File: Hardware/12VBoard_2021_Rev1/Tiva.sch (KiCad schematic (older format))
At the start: 2 parts

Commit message: Added Component Values.
Added values to high side buck and
 footprints to components.
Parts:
- renumbered Conn2 to Conn1, Conn3 to Conn2
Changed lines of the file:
@@
 	6150 2250 5800 2250
 $Comp
-L MRDT_Connectors:Molex_SL_05 Conn2
+L MRDT_Connectors:Molex_SL_05 Conn1
 U 1 1 5F976F73
 P 6350 1900
-F 0 "Conn2" H 6300 1850 60  0000 L CNN
+F 0 "Conn1" H 6300 1850 60  0000 L CNN
 F 1 "Molex_SL_05" H 6200 1750 60  0000 L CNN
 F 2 "MRDT_Connectors:MOLEX_SL_05_Horizontal" H 6350 1900 60  0001 C CNN
@@
 $EndComp
 $Comp
-L MRDT_Connectors:Molex_SL_07 Conn3
+L MRDT_Connectors:Molex_SL_07 Conn2
 U 1 1 5F97771C
 P 6350 2900
-F 0 "Conn3" H 6350 2850 60  0000 L CNN
+F 0 "Conn2" H 6350 2850 60  0000 L CNN
 F 1 "Molex_SL_07" H 6200 2750 60  0000 L CNN
 F 2 "MRDT_Connectors:MOLEX_SL_07_Horizontal" H 6350 3100 60  0001 C CNN

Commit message: Added Logic power circuits (High)
Added three smaller bucks for high current logic power and seprated acuation and logic pp
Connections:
- net DriveCTL: now reaches Conn2.7
- no-connect marks 1 -> 0
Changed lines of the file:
@@
 Text Notes 6450 1872 0    50   ~ 0
 Gimbal Sense (Analog Read)
-NoConn ~ 6150 2850
+Text HLabel 5800 2850 0    50   Output ~ 0
+DriveCTL
+Wire Wire Line
+	6150 2850 5800 2850
 $EndSCHEMATC

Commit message: Layout Started
Board dimensions
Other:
- note added: "Drive Board CTL (Digital Write)"
- note added: "Tiva 4 analog(current sense)/ \n7 toggles(digital write)"
- note removed: "Tiva 4 analog(current sense)/ \n5 toggles(digital write)"
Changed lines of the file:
@@
 $Descr A4 11693 8268
 encoding utf-8
-Sheet 2 8
+Sheet 8 8
 Title ""
 Date ""
@@
 $EndDescr
 Text Notes 5650 3450 0    79   ~ 0
-Tiva 4 analog(current sense)/ \n5 toggles(digital write)
+Tiva 4 analog(current sense)/ \n7 toggles(digital write)
 Text Notes 7480 1490 2    50   ~ 0
 Drive Sense (Analog Read)
@@
 Wire Wire Line
 	6150 2850 5800 2850
+Text Notes 7645 2880 2    50   ~ 0
+Drive Board CTL (Digital Write)
 $EndSCHEMATC

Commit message: Checked H pins
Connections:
- net DriveSense: no longer names the net of Conn1.1
- net MulitmediaSense renamed MultimediaSense
- no-connect marks 0 -> 1
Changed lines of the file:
@@
 EESchema Schematic File Version 4
-LIBS:12VBoard_2021_Rev1-cache
 EELAYER 30 0
 EELAYER END
@@
 Text Notes 6459 2385 0    49   ~ 0
 Gimbal CTL (Digital Write)
-Text HLabel 5800 1450 0    49   Input ~ 0
-DriveSense
-Wire Wire Line
-	6150 1450 5800 1450
 Text HLabel 5800 1550 0    49   Input ~ 0
 AuxMountSense
@@
 	6150 1550 5800 1550
 Text HLabel 5800 1650 0    49   Input ~ 0
-MulitmediaSense
+MultimediaSense
 Wire Wire Line
 	6150 1650 5800 1650
@@
 Text Notes 7645 2880 2    50   ~ 0
 Drive Board CTL (Digital Write)
+NoConn ~ 6150 1450
 $EndSCHEMATC

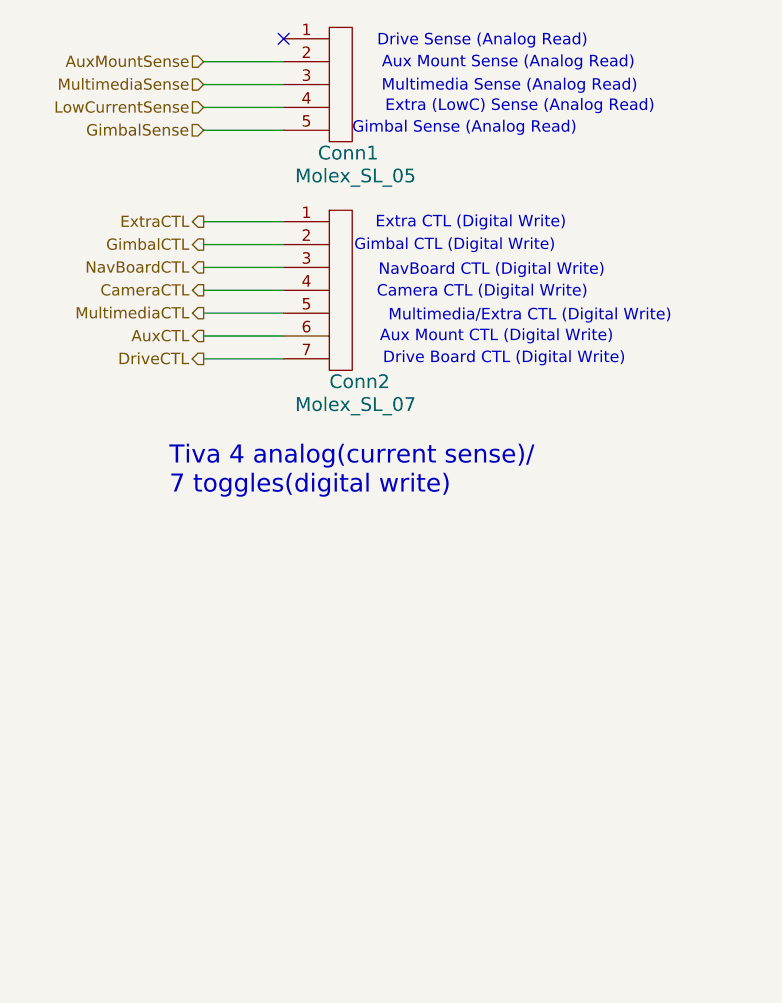
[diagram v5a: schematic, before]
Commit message: Changes!
Added the new correct connectors and redid all signal lines to the High Current side of the board. Also deleted all uncessacary components on the High current side that are no longer used.
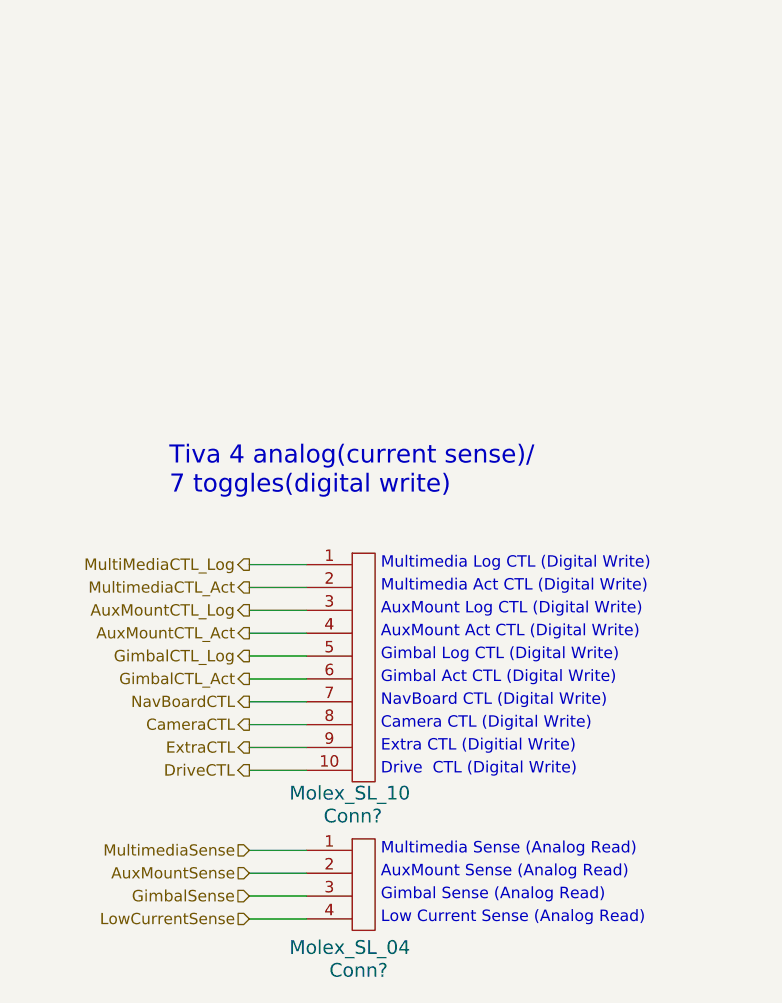
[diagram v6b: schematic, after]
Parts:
- removed Conn1: Molex_SL_05, MRDT_Connectors:MOLEX_SL_05_Horizontal, symbol MRDT_Connectors:Molex_SL_05
- removed Conn2: Molex_SL_07, MRDT_Connectors:MOLEX_SL_07_Horizontal, symbol MRDT_Connectors:Molex_SL_07
- added Conn?: Molex_SL_10, symbol MRDT_Connectors:Molex_SL_10
- added Conn?: Molex_SL_04, symbol MRDT_Connectors:Molex_SL_04
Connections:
- net AuxMountSense: now also Conn?.2
- net CameraCTL: now also Conn?.8
- net DriveCTL: now also Conn?.10
- net ExtraCTL: now also Conn?.9
- net GimbalSense: now also Conn?.3
- net LowCurrentSense: now also Conn?.4
- net MultimediaSense: now also Conn?.1
- net NavBoardCTL: now also Conn?.7
- new net AuxMountCTL_Act: Conn?.4
- new net AuxMountCTL_Log: Conn?.3
- new net GimbalCTL_Act: Conn?.6
- new net GimbalCTL_Log: Conn?.5
- new net MultiMediaCTL_Log: Conn?.1
- new net MultimediaCTL_Act: Conn?.2
- no-connect marks 1 -> 0
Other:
- note added: "AuxMount Act CTL (Digital Write)"
- note added: "AuxMount Log CTL (Digital Write)"
- note added: "AuxMount Sense (Analog Read)"
- note added: "Drive CTL (Digital Write)\n"
- note added: "Extra CTL (Digitial Write)"
- note added: "Gimbal Act CTL (Digital Write)"
- note added: "Gimbal Log CTL (Digital Write)"
- note added: "Low Current Sense (Analog Read)"
- note added: "Multimedia Act CTL (Digital Write)"
- note added: "Multimedia Log CTL (Digital Write)"
- note added: "Multimedia Sense (Analog Read)\n"
- note removed: "Aux Mount CTL (Digital Write)"
- note removed: "Aux Mount Sense (Analog Read)"
- note removed: "Drive Board CTL (Digital Write)"
- note removed: "Drive Sense (Analog Read)"
- note removed: "Extra (LowC) Sense (Analog Read)"
- note removed: "Extra CTL (Digital Write)"
- note removed: "Gimbal CTL (Digital Write)"
- note removed: "Multimedia Sense (Analog Read)"
- note removed: "Multimedia/Extra CTL (Digital Write)"
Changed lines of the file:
@@
 $Descr A4 11693 8268
 encoding utf-8
-Sheet 8 8
+Sheet 9 9
 Title ""
 Date ""
@@
 Text Notes 5650 3450 0    79   ~ 0
 Tiva 4 analog(current sense)/ \n7 toggles(digital write)
-Text Notes 7480 1490 2    50   ~ 0
-Drive Sense (Analog Read)
-Text Notes 7686 1586 2    50   ~ 0
-Aux Mount Sense (Analog Read)
-Text Notes 7698 1688 2    50   ~ 0
-Multimedia Sense (Analog Read)
-Text Notes 7773 1777 2    50   ~ 0
-Extra (LowC) Sense (Analog Read)
-Text Notes 7480 2589 2    50   ~ 0
-Camera CTL (Digital Write)
-Text Notes 7555 2494 2    50   ~ 0
-NavBoard CTL (Digital Write)
-Text Notes 7386 2286 2    50   ~ 0
-Extra CTL (Digital Write)
-Text Notes 7592 2784 2    50   ~ 0
-Aux Mount CTL (Digital Write)
-Text Notes 7847 2693 2    50   ~ 0
-Multimedia/Extra CTL (Digital Write)
-Text Notes 6459 2385 0    49   ~ 0
-Gimbal CTL (Digital Write)
-Text HLabel 5800 1550 0    49   Input ~ 0
+Text HLabel 6000 5100 0    49   Input ~ 0
 AuxMountSense
-Wire Wire Line
-	6150 1550 5800 1550
-Text HLabel 5800 1650 0    49   Input ~ 0
+Text HLabel 6000 5000 0    49   Input ~ 0
 MultimediaSense
-Wire Wire Line
-	6150 1650 5800 1650
-Text HLabel 5800 1750 0    49   Input ~ 0
+Text HLabel 6000 5300 0    49   Input ~ 0
 LowCurrentSense
-Wire Wire Line
-	6150 1750 5800 1750
-Wire Wire Line
-	6150 2350 5800 2350
-Wire Wire Line
-	6150 2450 5800 2450
-Text HLabel 5800 2550 0    49   Output ~ 0
+Text HLabel 6000 4450 0    49   Output ~ 0
 CameraCTL
-Wire Wire Line
-	6150 2550 5800 2550
-Text HLabel 5800 2650 0    49   Output ~ 0
-MultimediaCTL
-Wire Wire Line
-	6150 2650 5800 2650
-Text HLabel 5800 2750 0    49   Output ~ 0
-AuxCTL
-Wire Wire Line
-	6150 2750 5800 2750
-Text HLabel 5800 2450 0    49   Output ~ 0
+Text HLabel 6000 4350 0    49   Output ~ 0
 NavBoardCTL
-Text HLabel 5800 2350 0    49   Output ~ 0
-GimbalCTL
-Text HLabel 5800 2250 0    49   Output ~ 0
+Text HLabel 6000 4550 0    49   Output ~ 0
 ExtraCTL
-Wire Wire Line
-	6150 2250 5800 2250
+Text HLabel 6000 5200 0    50   Input ~ 0
+GimbalSense
+Text HLabel 6000 4650 0    50   Output ~ 0
+DriveCTL
 $Comp
-L MRDT_Connectors:Molex_SL_05 Conn1
-U 1 1 5F976F73
-P 6350 1900
-F 0 "Conn1" H 6300 1850 60  0000 L CNN
-F 1 "Molex_SL_05" H 6200 1750 60  0000 L CNN
-F 2 "MRDT_Connectors:MOLEX_SL_05_Horizontal" H 6350 1900 60  0001 C CNN
-F 3 "" H 6350 1900 60  0001 C CNN
-	1    6350 1900
+L MRDT_Connectors:Molex_SL_10 Conn?
+U 1 1 5FB5A813
+P 6450 4700
+F 0 "Conn?" H 6325 4550 60  0000 L CNN
+F 1 "Molex_SL_10" H 6175 4650 60  0000 L CNN
+F 2 "" H 6450 5200 60  0001 C CNN
+F 3 "" H 6450 5200 60  0001 C CNN
+	1    6450 4700
 	1    0    0    -1
 $EndComp
 $Comp
-L MRDT_Connectors:Molex_SL_07 Conn2
-U 1 1 5F97771C
-P 6350 2900
-F 0 "Conn2" H 6350 2850 60  0000 L CNN
-F 1 "Molex_SL_07" H 6200 2750 60  0000 L CNN
-F 2 "MRDT_Connectors:MOLEX_SL_07_Horizontal" H 6350 3100 60  0001 C CNN
-F 3 "" H 6350 3100 60  0001 C CNN
-	1    6350 2900
+L MRDT_Connectors:Molex_SL_04 Conn?
+U 1 1 5FB5B79F
+P 6450 5350
+F 0 "Conn?" H 6350 5175 60  0000 L CNN
+F 1 "Molex_SL_04" H 6175 5275 60  0000 L CNN
+F 2 "" H 6450 5350 60  0001 C CNN
+F 3 "" H 6450 5350 60  0001 C CNN
+	1    6450 5350
 	1    0    0    -1
 $EndComp
-Text HLabel 5800 1850 0    50   Input ~ 0
-GimbalSense
+Text Notes 6575 3875 0    50   ~ 0
+Multimedia Act CTL (Digital Write)
+Text Notes 6575 3775 0    50   ~ 0
+Multimedia Log CTL (Digital Write)
+Text Notes 6575 4075 0    50   ~ 0
+AuxMount Act CTL (Digital Write)
+Text Notes 6575 3975 0    50   ~ 0
+AuxMount Log CTL (Digital Write)
+Text Notes 6575 4275 0    50   ~ 0
+Gimbal Act CTL (Digital Write)
+Text Notes 6575 4175 0    50   ~ 0
+Gimbal Log CTL (Digital Write)
+Text Notes 6575 4375 0    50   ~ 0
+NavBoard CTL (Digital Write)
+Text Notes 6575 4475 0    50   ~ 0
+Camera CTL (Digital Write)
+Text Notes 6575 4575 0    50   ~ 0
+Extra CTL (Digitial Write)
+Text Notes 6575 4675 0    50   ~ 0
+Drive  CTL (Digital Write)\n
+Text Notes 6575 5125 0    50   ~ 0
+AuxMount Sense (Analog Read)
+Text Notes 6575 5025 0    50   ~ 0
+Multimedia Sense (Analog Read)\n
+Text Notes 6575 5225 0    50   ~ 0
+Gimbal Sense (Analog Read)
+Text Notes 6575 5325 0    50   ~ 0
+Low Current Sense (Analog Read)
 Wire Wire Line
-	6150 1850 5800 1850
-Text Notes 6450 1872 0    50   ~ 0
-Gimbal Sense (Analog Read)
-Text HLabel 5800 2850 0    50   Output ~ 0
-DriveCTL
+	6000 5000 6250 5000
 Wire Wire Line
-	6150 2850 5800 2850
-Text Notes 7645 2880 2    50   ~ 0
-Drive Board CTL (Digital Write)
-NoConn ~ 6150 1450
+	6000 5100 6250 5100
+Wire Wire Line
+	6000 5200 6250 5200
+Wire Wire Line
+	6000 5300 6250 5300
+Text HLabel 6000 4050 0    49   Output ~ 0
+AuxMountCTL_Act
+Text HLabel 6000 4250 0    49   Output ~ 0
+GimbalCTL_Act
+Text HLabel 6000 3850 0    49   Output ~ 0
+MultimediaCTL_Act
+Wire Wire Line
+	6000 4350 6250 4350
+Wire Wire Line
+	6000 4450 6250 4450
+Wire Wire Line
+	6000 4550 6250 4550
+Wire Wire Line
+	6000 4650 6250 4650
+Text HLabel 6000 3750 0    50   Output ~ 0
+MultiMediaCTL_Log
+Text HLabel 6000 3950 0    50   Output ~ 0
+AuxMountCTL_Log
+Text HLabel 6000 4150 0    50   Output ~ 0
+GimbalCTL_Log
+Wire Wire Line
+	6000 4250 6250 4250
+Wire Wire Line
+	6000 4150 6250 4150
+Wire Wire Line
+	6000 4050 6250 4050
+Wire Wire Line
+	6000 3950 6250 3950
+Wire Wire Line
+	6000 3850 6250 3850
+Wire Wire Line
+	6000 3750 6250 3750
 $EndSCHEMATC

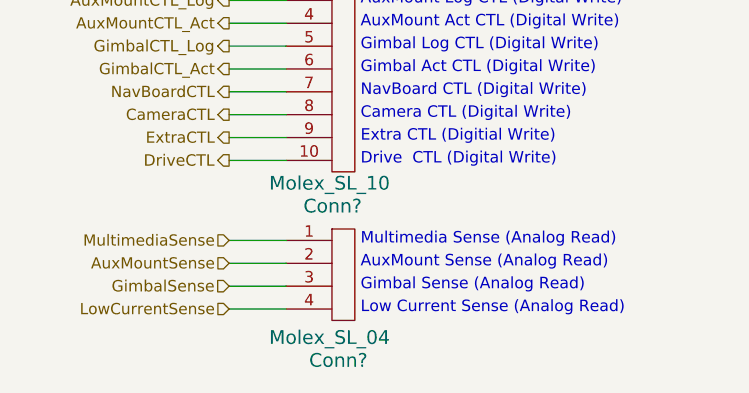
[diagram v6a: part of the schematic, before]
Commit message: Redesigned low current ports schematic
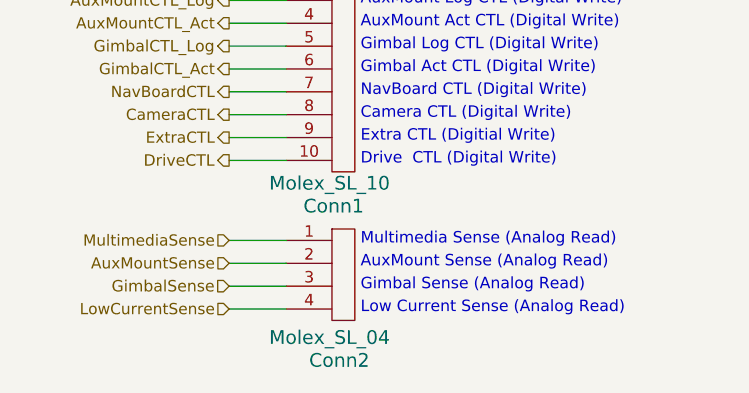
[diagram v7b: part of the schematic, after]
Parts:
- Conn1: renamed from Conn?; footprint (none) -> MRDT_Connectors:MOLEX_SL_10_Horizontal
- Conn2: renamed from Conn?; footprint (none) -> MRDT_Connectors:MOLEX_SL_04_Horizontal
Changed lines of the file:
@@
 DriveCTL
 $Comp
-L MRDT_Connectors:Molex_SL_10 Conn?
+L MRDT_Connectors:Molex_SL_10 Conn1
 U 1 1 5FB5A813
 P 6450 4700
-F 0 "Conn?" H 6325 4550 60  0000 L CNN
+F 0 "Conn1" H 6325 4550 60  0000 L CNN
 F 1 "Molex_SL_10" H 6175 4650 60  0000 L CNN
-F 2 "" H 6450 5200 60  0001 C CNN
+F 2 "MRDT_Connectors:MOLEX_SL_10_Horizontal" H 6450 5200 60  0001 C CNN
 F 3 "" H 6450 5200 60  0001 C CNN
 	1    6450 4700
@@
 $EndComp
 $Comp
-L MRDT_Connectors:Molex_SL_04 Conn?
+L MRDT_Connectors:Molex_SL_04 Conn2
 U 1 1 5FB5B79F
 P 6450 5350
-F 0 "Conn?" H 6350 5175 60  0000 L CNN
+F 0 "Conn2" H 6350 5175 60  0000 L CNN
 F 1 "Molex_SL_04" H 6175 5275 60  0000 L CNN
-F 2 "" H 6450 5350 60  0001 C CNN
+F 2 "MRDT_Connectors:MOLEX_SL_04_Horizontal" H 6450 5350 60  0001 C CNN
 F 3 "" H 6450 5350 60  0001 C CNN
 	1    6450 5350
